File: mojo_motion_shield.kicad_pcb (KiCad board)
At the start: 2 copper layers, 77.6 x 87 mm, 36 parts, among them J1 SERVO, J10 ENC, J11 MSX, J12 MSX, J13 MSX, J14 MSX, J15 MSX, J16 MSX, J17 ENC, J18 ENC, J19 SSERIAL0, J2 ANALOG, J20 SSERIAL1, J3 POWER, J4 ENC, J5 HOST, J6 SPI0, J7 SPI1, J8 ENC, J9 ENC, P1 MOJO, U1 TB67S2X9FTG, U2 TB67S2X9FTG, U3 TB67S2X9FTG, U4 TB67S2X9FTG, U5 TB67S2X9FTG, U6 TB67S2X9FTG

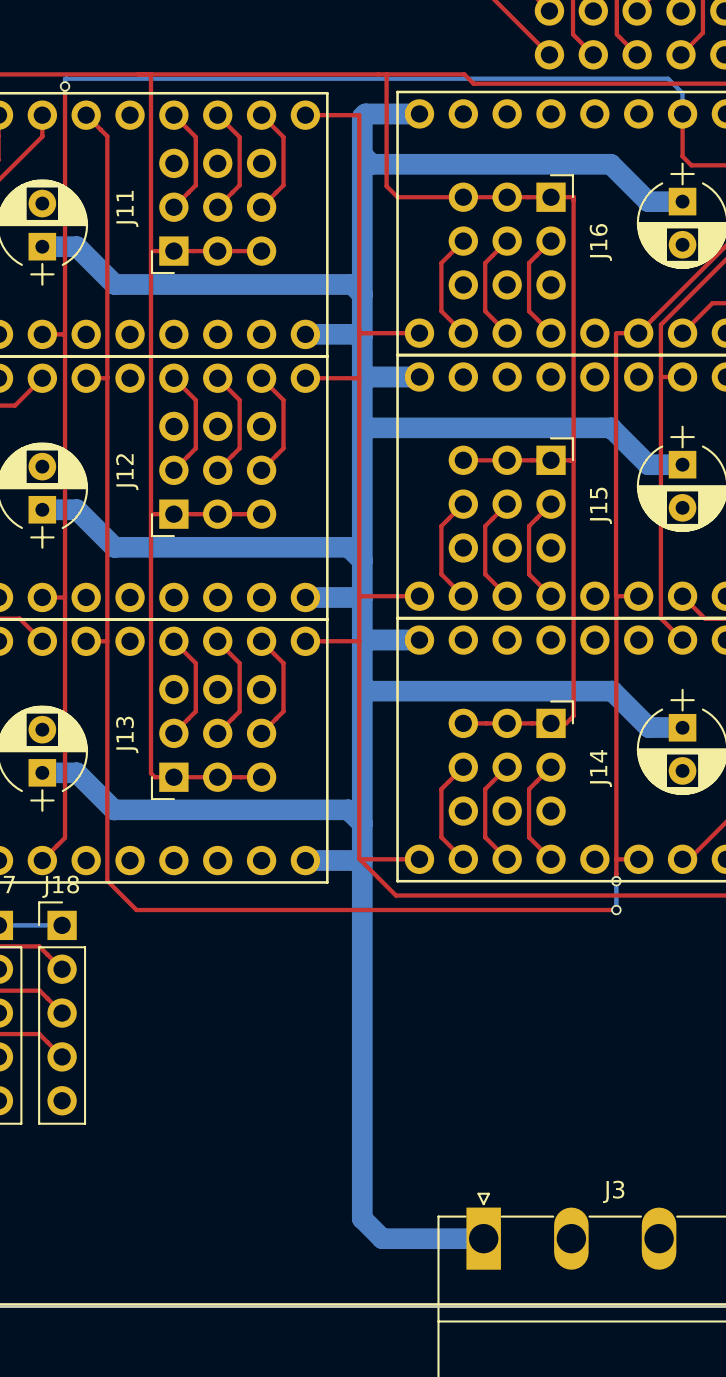
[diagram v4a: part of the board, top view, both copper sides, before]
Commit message: increase common motor power track width
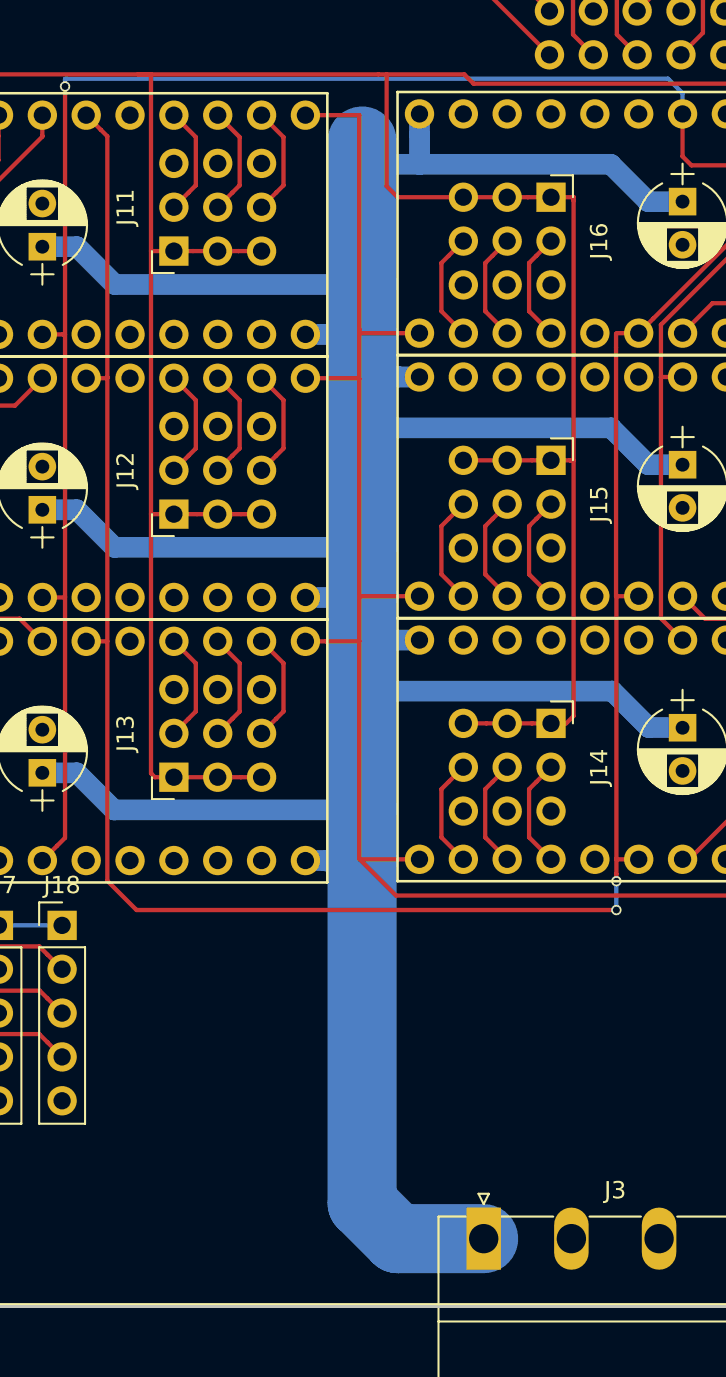
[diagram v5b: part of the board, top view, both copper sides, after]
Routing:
- net +12V: track 209.3 -> 205.5 mm
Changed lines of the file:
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@@
     (thickness 1.6)
     (drawings 17)
-    (tracks 618)
+    (tracks 626)
     (zones 0)
     (modules 36)
@@
   (gr_line (start 105.791 135.255) (end 105.791 60.96) (layer Edge.Cuts) (width 0.15))
   (gr_line (start 144.78 50.8) (end 180.9 50.79) (layer Edge.Cuts) (width 0.15))
-  (segment (start 142.7 68.89) (end 142.888657 68.701343) (width 1.2) (layer B.Cu) (net 1))
-  (segment (start 142.888657 68.701343) (end 146.013379 68.701343) (width 1.2) (layer B.Cu) (net 1))
-  (segment (start 142.778657 83.941343) (end 146.013379 83.941343) (width 1.2) (layer B.Cu) (net 1))
   (segment (start 142.7 84.02) (end 142.778657 83.941343) (width 1.2) (layer B.Cu) (net 1))
-  (segment (start 142.696738 96.713262) (end 139.405334 96.713262) (width 1.2) (layer B.Cu) (net 1))
   (segment (start 142.7 96.71) (end 142.696738 96.713262) (width 1.2) (layer B.Cu) (net 1))
-  (segment (start 142.758657 99.181343) (end 146.013379 99.181343) (width 1.2) (layer B.Cu) (net 1))
   (segment (start 142.7 99.24) (end 142.758657 99.181343) (width 1.2) (layer B.Cu) (net 1))
-  (segment (start 142.7 99.24) (end 142.7 96.71) (width 1.2) (layer B.Cu) (net 1))
-  (segment (start 142.636738 111.953262) (end 139.405334 111.953262) (width 1.2) (layer B.Cu) (net 1))
   (segment (start 142.7 111.89) (end 142.636738 111.953262) (width 1.2) (layer B.Cu) (net 1))
-  (segment (start 142.7 101.8) (end 142.7 99.24) (width 1.2) (layer B.Cu) (net 1))
-  (segment (start 142.7 111.89) (end 142.7 109.82) (width 1.2) (layer B.Cu) (net 1))
-  (segment (start 142.7 109.82) (end 142.7 101.8) (width 1.2) (layer B.Cu) (net 1))
-  (segment (start 142.7 96.71) (end 142.7 94.59) (width 1.2) (layer B.Cu) (net 1))
-  (segment (start 142.7 94.59) (end 142.7 86.63) (width 1.2) (layer B.Cu) (net 1))
-  (segment (start 142.7 86.63) (end 142.7 84.02) (width 1.2) (layer B.Cu) (net 1))
-  (segment (start 142.623262 81.473262) (end 139.405334 81.473262) (width 1.2) (layer B.Cu) (net 1))
-  (segment (start 142.7 81.55) (end 142.623262 81.473262) (width 1.2) (layer B.Cu) (net 1))
-  (segment (start 142.7 84.02) (end 142.7 81.55) (width 1.2) (layer B.Cu) (net 1))
-  (segment (start 142.7 81.55) (end 142.7 79.17) (width 1.2) (layer B.Cu) (net 1))
-  (segment (start 142.7 79.17) (end 142.7 71.07) (width 1.2) (layer B.Cu) (net 1))
-  (segment (start 142.7 71.07) (end 142.7 68.89) (width 1.2) (layer B.Cu) (net 1))
   (segment (start 161.242036 104.25) (end 161.253379 104.261343) (width 1.2) (layer B.Cu) (net 1))
   (segment (start 159.3 104.25) (end 161.242036 104.25) (width 1.2) (layer B.Cu) (net 1))
   (segment (start 157.19 102.14) (end 159.3 104.25) (width 1.2) (layer B.Cu) (net 1))
-  (segment (start 142.7 101.8) (end 143.04 102.14) (width 1.2) (layer B.Cu) (net 1))
-  (segment (start 143.04 102.14) (end 157.19 102.14) (width 1.2) (layer B.Cu) (net 1))
-  (segment (start 142.7 86.63) (end 142.96 86.89) (width 1.2) (layer B.Cu) (net 1))
   (segment (start 159.253379 89.021343) (end 161.253379 89.021343) (width 1.2) (layer B.Cu) (net 1))
   (segment (start 157.122036 86.89) (end 159.253379 89.021343) (width 1.2) (layer B.Cu) (net 1))
-  (segment (start 142.96 86.89) (end 157.122036 86.89) (width 1.2) (layer B.Cu) (net 1))
   (segment (start 159.253379 73.781343) (end 161.253379 73.781343) (width 1.2) (layer B.Cu) (net 1))
   (segment (start 157.092036 71.62) (end 159.253379 73.781343) (width 1.2) (layer B.Cu) (net 1))
-  (segment (start 142.7 71.07) (end 143.25 71.62) (width 1.2) (layer B.Cu) (net 1))
-  (segment (start 143.25 71.62) (end 157.092036 71.62) (width 1.2) (layer B.Cu) (net 1))
   (segment (start 126.165334 106.873262) (end 124.165334 106.873262) (width 1.2) (layer B.Cu) (net 1))
   (segment (start 128.312072 109.02) (end 126.165334 106.873262) (width 1.2) (layer B.Cu) (net 1))
-  (segment (start 142.7 109.82) (end 141.9 109.02) (width 1.2) (layer B.Cu) (net 1))
-  (segment (start 141.9 109.02) (end 128.312072 109.02) (width 1.2) (layer B.Cu) (net 1))
   (segment (start 128.342072 93.81) (end 126.165334 91.633262) (width 1.2) (layer B.Cu) (net 1))
   (segment (start 126.165334 91.633262) (end 124.165334 91.633262) (width 1.2) (layer B.Cu) (net 1))
-  (segment (start 142.7 94.59) (end 141.92 93.81) (width 1.2) (layer B.Cu) (net 1))
-  (segment (start 141.92 93.81) (end 128.342072 93.81) (width 1.2) (layer B.Cu) (net 1))
   (segment (start 126.165334 76.393262) (end 124.165334 76.393262) (width 1.2) (layer B.Cu) (net 1))
   (segment (start 128.352072 78.58) (end 126.165334 76.393262) (width 1.2) (layer B.Cu) (net 1))
-  (segment (start 142.7 79.17) (end 142.11 78.58) (width 1.2) (layer B.Cu) (net 1))
-  (segment (start 142.11 78.58) (end 128.352072 78.58) (width 1.2) (layer B.Cu) (net 1))
-  (segment (start 142.7 132.7) (end 142.7 111.89) (width 1.2) (layer B.Cu) (net 1))
-  (segment (start 149.733 133.858) (end 143.858 133.858) (width 1.2) (layer B.Cu) (net 1))
-  (segment (start 143.858 133.858) (end 142.7 132.7) (width 1.2) (layer B.Cu) (net 1))
+  (segment (start 144.733 133.858) (end 142.69 131.815) (width 4) (layer B.Cu) (net 1))
+  (segment (start 149.733 133.858) (end 144.733 133.858) (width 4) (layer B.Cu) (net 1))
+  (segment (start 146.013379 69.903424) (end 146.02 69.910045) (width 1.2) (layer B.Cu) (net 1))
+  (segment (start 146.02 69.910045) (end 146.02 71.62) (width 1.2) (layer B.Cu) (net 1))
+  (segment (start 146.013379 68.701343) (end 146.013379 69.903424) (width 1.2) (layer B.Cu) (net 1))
+  (segment (start 143.25 71.62) (end 146.02 71.62) (width 1.2) (layer B.Cu) (net 1))
+  (segment (start 146.02 71.62) (end 157.092036 71.62) (width 1.2) (layer B.Cu) (net 1))
+  (segment (start 142.66 78.58) (end 142.69 78.55) (width 1.2) (layer B.Cu) (net 1))
+  (segment (start 128.352072 78.58) (end 142.66 78.58) (width 1.2) (layer B.Cu) (net 1))
+  (segment (start 142.69 78.55) (end 142.69 70.27) (width 4) (layer B.Cu) (net 1))
+  (segment (start 139.405334 81.473262) (end 142.656738 81.473262) (width 1.2) (layer B.Cu) (net 1))
+  (segment (start 142.656738 81.473262) (end 142.69 81.44) (width 1.2) (layer B.Cu) (net 1))
+  (segment (start 142.69 81.44) (end 142.69 78.55) (width 4) (layer B.Cu) (net 1))
+  (segment (start 142.69 83.92) (end 142.69 81.44) (width 4) (layer B.Cu) (net 1))
+  (segment (start 142.711343 83.941343) (end 142.69 83.92) (width 1.2) (layer B.Cu) (net 1))
+  (segment (start 142.69 86.95) (end 142.69 83.92) (width 4) (layer B.Cu) (net 1))
+  (segment (start 142.69 93.75) (end 142.69 86.95) (width 4) (layer B.Cu) (net 1))
+  (segment (start 142.663262 111.953262) (end 142.69 111.98) (width 1.2) (layer B.Cu) (net 1))
+  (segment (start 142.69 131.815) (end 142.69 111.98) (width 4) (layer B.Cu) (net 1))
+  (segment (start 142.69 111.98) (end 142.69 108.95) (width 4) (layer B.Cu) (net 1))
+  (segment (start 142.69 108.95) (end 142.69 102.29) (width 4) (layer B.Cu) (net 1))
+  (segment (start 142.84 102.14) (end 142.69 102.29) (width 1.2) (layer B.Cu) (net 1))
+  (segment (start 157.19 102.14) (end 142.84 102.14) (width 1.2) (layer B.Cu) (net 1))
+  (segment (start 142.691343 99.181343) (end 142.69 99.18) (width 1.2) (layer B.Cu) (net 1))
+  (segment (start 146.013379 99.181343) (end 142.691343 99.181343) (width 1.2) (layer B.Cu) (net 1))
+  (segment (start 142.69 102.29) (end 142.69 99.18) (width 4) (layer B.Cu) (net 1))
+  (segment (start 142.666738 96.713262) (end 142.69 96.69) (width 1.2) (layer B.Cu) (net 1))
+  (segment (start 139.405334 96.713262) (end 142.666738 96.713262) (width 1.2) (layer B.Cu) (net 1))
+  (segment (start 142.69 99.18) (end 142.69 96.69) (width 4) (layer B.Cu) (net 1))
+  (segment (start 142.69 96.69) (end 142.69 93.75) (width 4) (layer B.Cu) (net 1))
+  (segment (start 142.63 93.81) (end 142.69 93.75) (width 1.2) (layer B.Cu) (net 1))
+  (segment (start 128.342072 93.81) (end 142.63 93.81) (width 1.2) (layer B.Cu) (net 1))
+  (segment (start 142.62 109.02) (end 142.69 108.95) (width 1.2) (layer B.Cu) (net 1))
+  (segment (start 128.312072 109.02) (end 142.62 109.02) (width 1.2) (layer B.Cu) (net 1))
+  (segment (start 142.75 86.89) (end 142.69 86.95) (width 1.2) (layer B.Cu) (net 1))
+  (segment (start 157.122036 86.89) (end 142.75 86.89) (width 1.2) (layer B.Cu) (net 1))
+  (segment (start 144.811298 83.941343) (end 144.789955 83.92) (width 1.2) (layer B.Cu) (net 1))
+  (segment (start 144.789955 83.92) (end 142.69 83.92) (width 1.2) (layer B.Cu) (net 1))
+  (segment (start 146.013379 83.941343) (end 144.811298 83.941343) (width 1.2) (layer B.Cu) (net 1))
+  (segment (start 140.607415 111.953262) (end 140.634153 111.98) (width 1.2) (layer B.Cu) (net 1))
+  (segment (start 140.634153 111.98) (end 142.69 111.98) (width 1.2) (layer B.Cu) (net 1))
+  (segment (start 139.405334 111.953262) (end 140.607415 111.953262) (width 1.2) (layer B.Cu) (net 1))
   (segment (start 170.09 107.951998) (end 170.853998 107.188) (width 0.25) (layer F.Cu) (net 3))
   (segment (start 172.72 107.188) (end 173.863 106.045) (width 0.25) (layer F.Cu) (net 3))

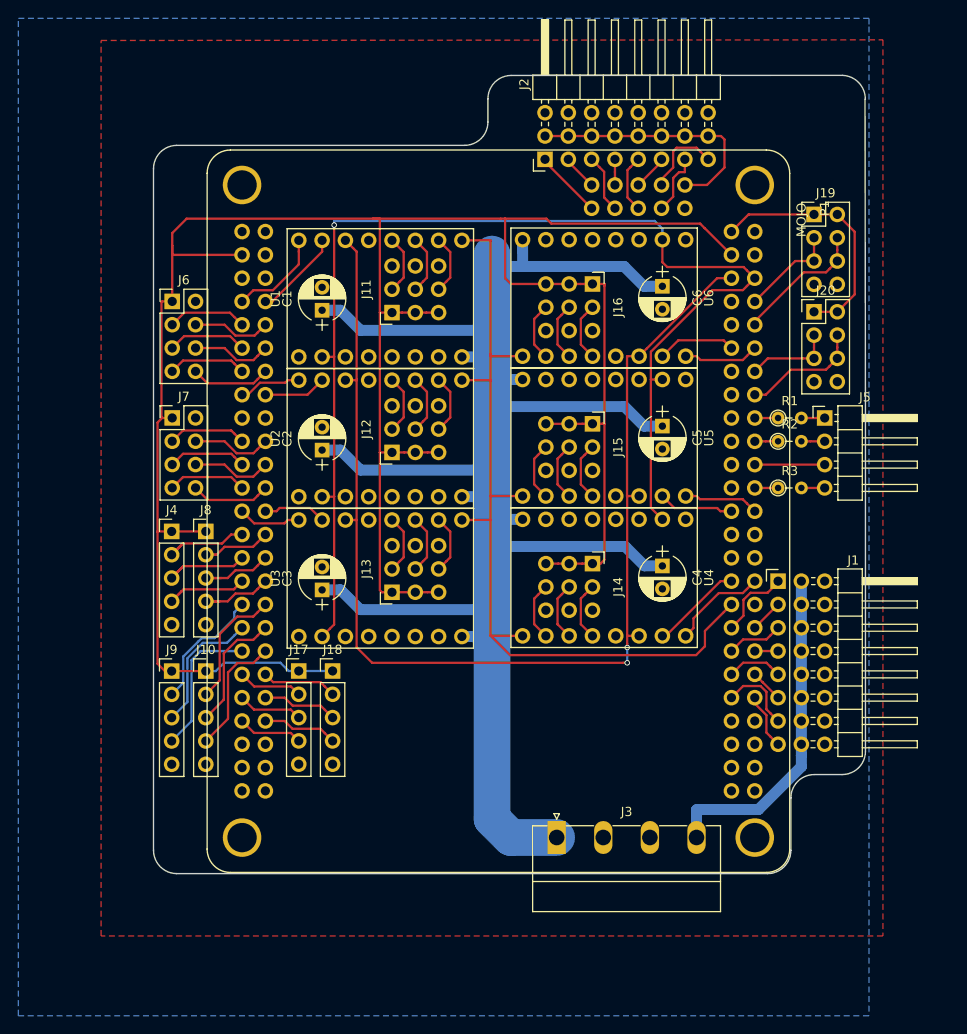
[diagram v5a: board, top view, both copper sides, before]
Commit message: refactor port positions
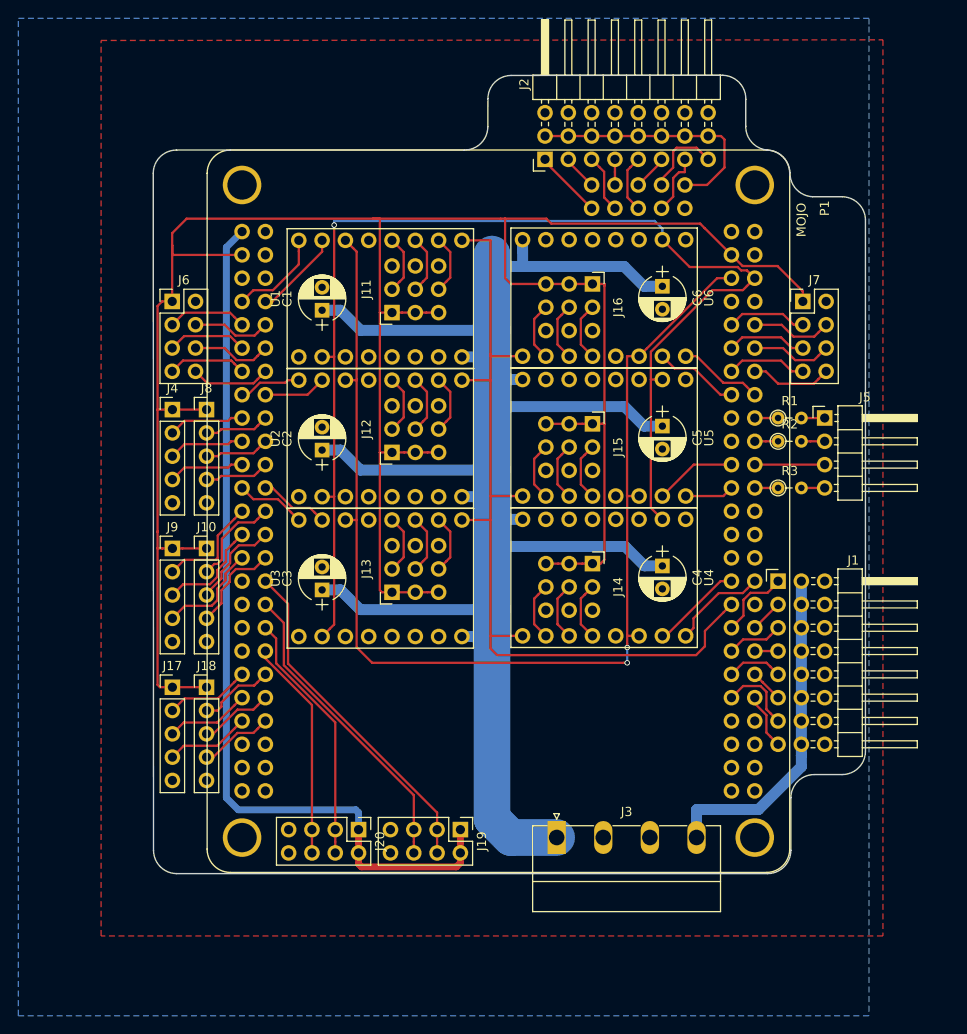
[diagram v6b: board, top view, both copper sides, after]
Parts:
- moved J19 77.3 mm to (139.2, 133.0), turned to 270 degrees
- moved J20 75.2 mm to (128.1, 133.0), turned to 270 degrees
- moved J7 69.9 mm to (176.6, 75.4)
- moved J17 13.9 mm to (107.8, 117.5)
- moved J18 13.9 mm to (111.6, 117.5)
- moved J10 13.4 mm to (111.6, 102.3)
- moved J9 13.4 mm to (107.8, 102.3)
- moved J4 13.3 mm to (107.8, 87.2)
- moved J8 13.3 mm to (111.6, 87.2)
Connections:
- J19 pad 4: /SS0RX -> /SS0TX
- J19 pad 5: /SS0TX -> /SS0RX
- J20 pad 4: /SS1RX -> /SS1TX
- J20 pad 5: /SS1TX -> /SS1RX
- P1 pad 100: /YENC_B -> /AENC_I
- P1 pad 101: /XENC_I -> (no net)
- P1 pad 102: /YENC_I -> /SS0TX
- P1 pad 104: /ZENC_A -> (no net)
- P1 pad 105: /AENC_A -> /SS0RX
- P1 pad 11: /BSTEP -> (no net)
- P1 pad 111: /ZENC_B -> (no net)
- P1 pad 112: /AENC_B -> /SS1TX
- P1 pad 114: /ZENC_I -> (no net)
- P1 pad 115: /AENC_I -> /SS1RX
- P1 pad 12: /BDIR -> (no net)
- P1 pad 14: (no net) -> /BDIR
- P1 pad 16: (no net) -> /BSTEP
- P1 pad 26: (no net) -> /CSTEP
- P1 pad 27: /SS1RX -> /CDIR
- P1 pad 29: (no net) -> /CS5
- P1 pad 30: /SS1TX -> /SPI1_CLK
- P1 pad 32: /CSTEP -> /CS4
- P1 pad 33: /CDIR -> /SPI1_IN
- P1 pad 34: (no net) -> /CS3
- P1 pad 35: /SS0RX -> /SPI1_OUT
- P1 pad 41: /SS0TX -> (no net)
- P1 pad 82: (no net) -> /XENC_A
- P1 pad 83: (no net) -> /YENC_A
- P1 pad 84: /CS3 -> /XENC_B
- P1 pad 85: /SPI1_OUT -> /YENC_B
- P1 pad 87: /CS4 -> /XENC_I
- P1 pad 88: /SPI1_IN -> /YENC_I
- P1 pad 92: /CS5 -> /ZDIR
- P1 pad 93: /SPI1_CLK -> /ZSTEP
- P1 pad 94: /ZDIR -> /ZENC_A
- P1 pad 95: /ZSTEP -> /AENC_A
- P1 pad 97: /XENC_A -> /ZENC_B
- P1 pad 98: /YENC_A -> /AENC_B
- P1 pad 99: /XENC_B -> /ZENC_I
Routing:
- net +5V: track 27.0 -> 98.1 mm
- net /SS0TX: track 10.8 -> 37.4 mm
- net /SS0RX: track 14.6 -> 33.8 mm
- net /SS1TX: track 9.58 -> 27.7 mm
- net /SS1RX: track 13.2 -> 24.1 mm
- net /ZENC_I: track 15.6 -> 11.5 mm
- net /AENC_B: track 13.5 -> 10.3 mm
- net /AENC_I: track 13.5 -> 10.4 mm
- net /ZENC_B: track 14.5 -> 11.4 mm
- net /AENC_A: track 13.5 -> 10.5 mm
- net /BDIR: track 8.22 -> 5.36 mm
- net +3V3: track 267.9 -> 270.3 mm
- net /BENC_I: track 7.08 -> 9.23 mm
- net /BENC_B: track 7.08 -> 9.23 mm
- net /BENC_A: track 7.08 -> 9.23 mm
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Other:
- outline, holes or cut-outs redrawn
